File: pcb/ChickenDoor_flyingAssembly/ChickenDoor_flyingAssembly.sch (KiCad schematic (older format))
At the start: 27 parts

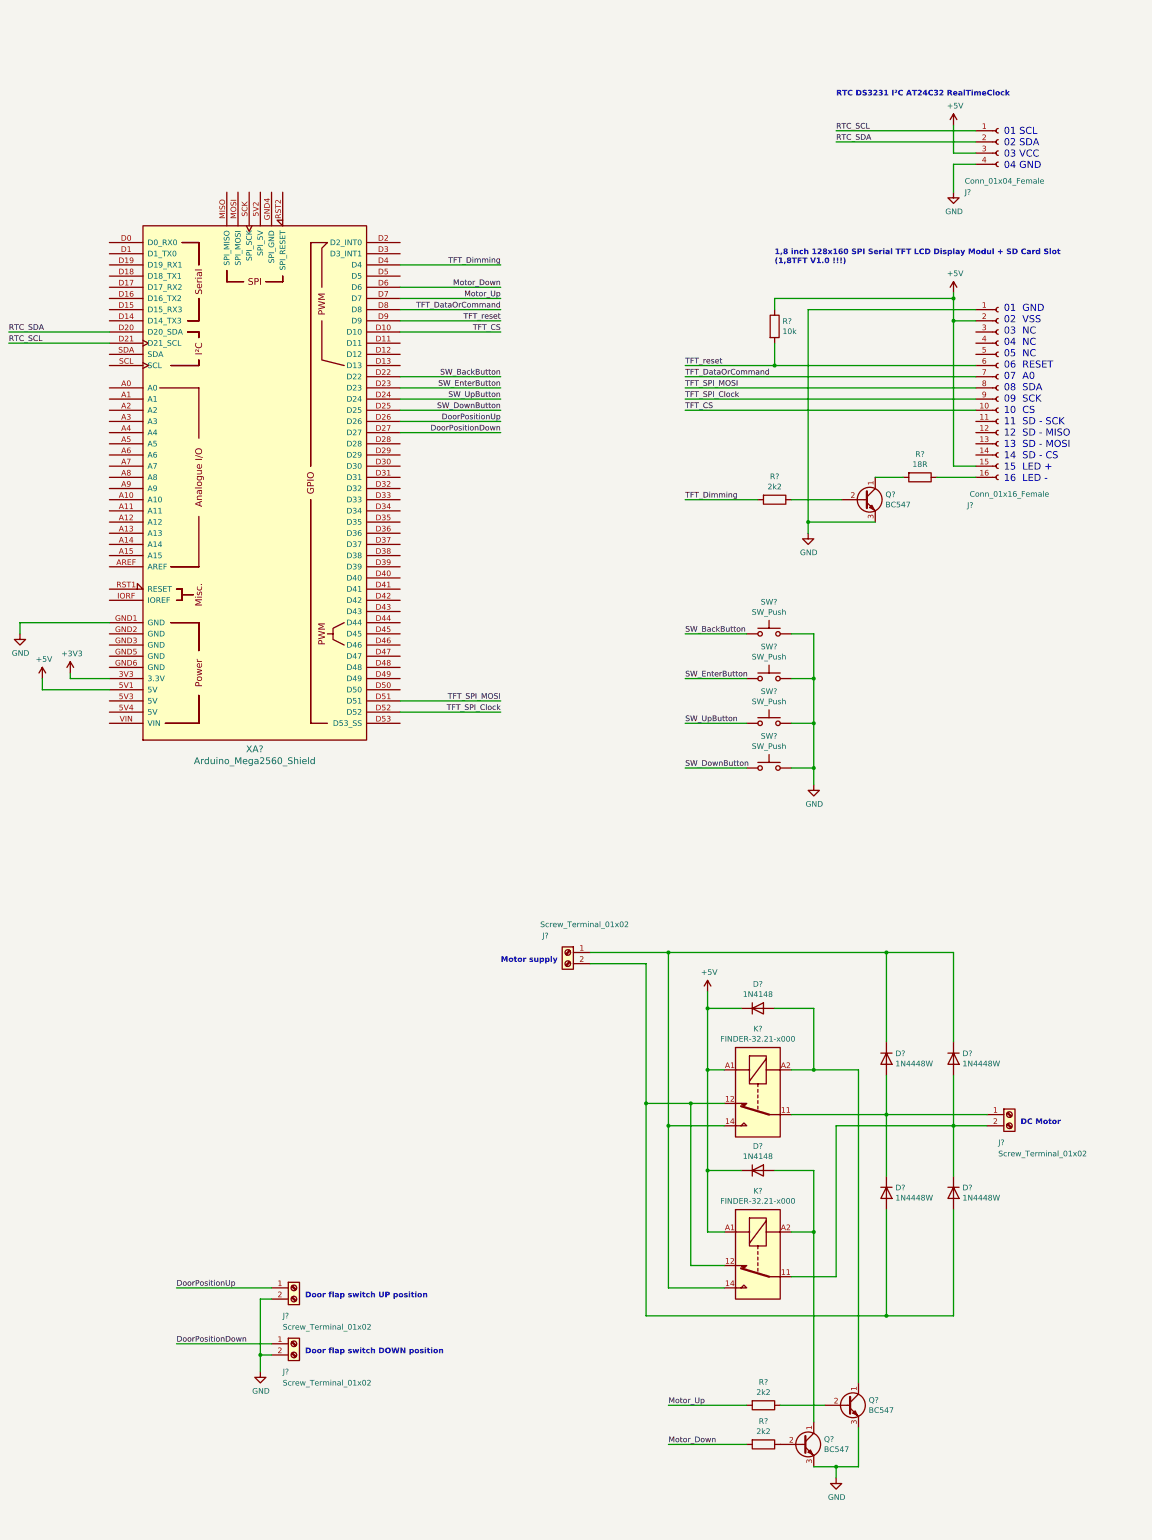
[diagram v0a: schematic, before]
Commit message: Added hardware components to control a 'indoor lighting' into the schematic.
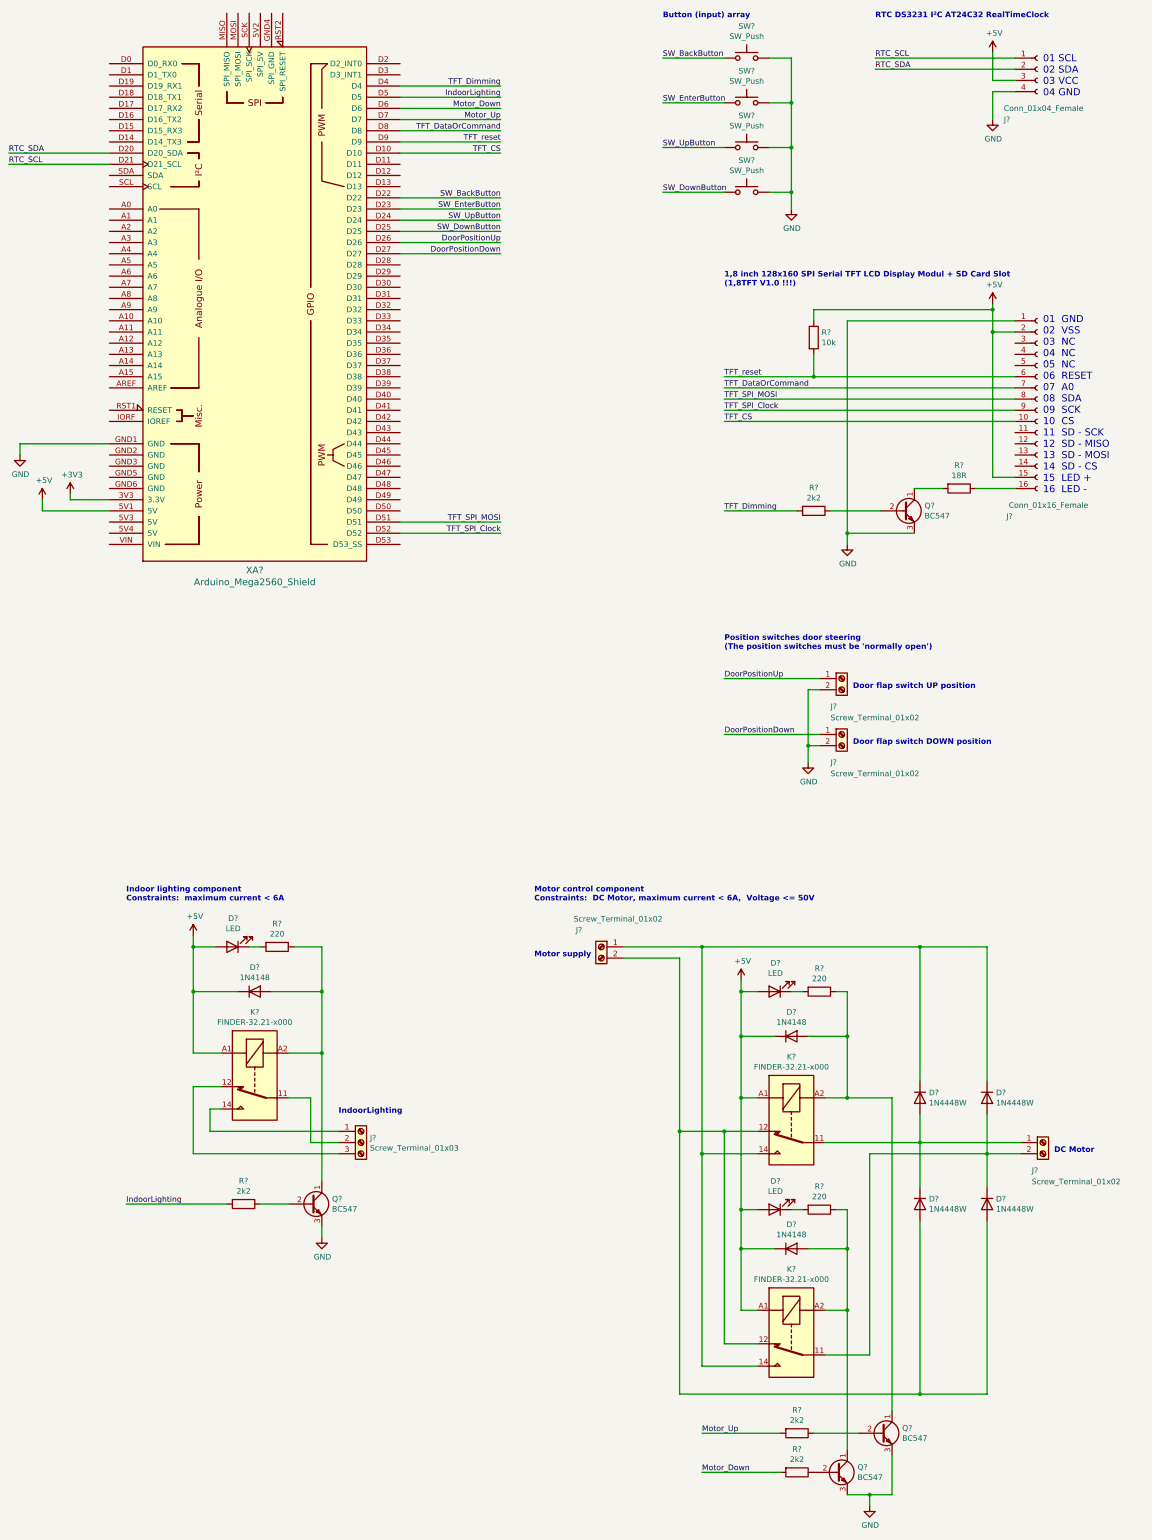
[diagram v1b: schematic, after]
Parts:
- added D? (x3): LED, symbol Device:LED
- added D?: 1N4148, Diode_THT:D_DO-35_SOD27_P7.62mm_Horizontal, symbol Diode:1N4148
- added J?: Screw_Terminal_01x03, symbol Connector:Screw_Terminal_01x03
- added K?: FINDER-32.21-x000, Relay_THT:Relay_SPST_Finder_32.21-x300, symbol Relay:FINDER-32.21-x000
- added Q?: BC547, Package_TO_SOT_THT:TO-92_Inline, symbol Transistor_BJT:BC547
- added R? (x3): 220, symbol Device:R
- added R?: 2k2, symbol Device:R
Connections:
- net +5V: now also D?.1 (K), D?.2 (A), D?.2 (A), D?.2 (A), K?.A1
- net GND: now also Q?.3 (E)
- net IndoorLighting: now reaches XA?.D5
- net IndoorLighting: now also R?.2
- net at D?.2 (A), K?.A2, Q?.1 (C): now also R?.1 (x2)
- new net: D?.1 (K), R?.2 (x3)
- new net: J?.2 (Pin_2), K?.11
- new net: J?.3 (Pin_3), K?.12
- new net: J?.1 (Pin_1), K?.14
- new net: D?.2 (A), K?.A2, Q?.1 (C), R?.1
- new net: Q?.2 (B), R?.1
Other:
- note added: "Button (input) array"
- note added: "Indoor lighting component\nConstraints: maximum current < 6A"
- note added: "IndoorLighting"
- note added: "Motor control component\nConstraints: DC Motor, maximum current < 6A, Voltage <= 50V"
- note added: "Position switches door steering\n(The position switches must be 'normally open')"
- moved on the sheet: D?, J?, K?, Q?, R?, SW?, XA?
